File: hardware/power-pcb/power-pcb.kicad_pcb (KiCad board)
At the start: 2 copper layers, 165 x 48 mm, 71 parts, among them J1 XT60PW-M-AS, J10 Molex_MicroFit-3.0_4x1, J11 Molex_MicroFit-3.0_4x1, J12 Molex_MicroFit-3.0_4x1, J2 XT30, J3 MicroFit2x12_Odd_Even, J4 MicroFit2x12_CouterClockwise, J5 XT30, J6 XT30, J7 XT60PW-M-AS, J8 JST_XH_5, J9 Molex_MicroFit-3.0_4x1, Q1 SQJ138EP-T1_GE3, Q2 SQJ138EP-T1_GE3, U1 BTS50010-1TAD, U2 LTC4365TS8, U3 R-78E3.3-1.0, U4 BTT_TMC5160T_Pro, U5 BTT_TMC5160T_Pro, U6 BTT_TMC5160T_Pro, U7 BTT_TMC5160T_Pro

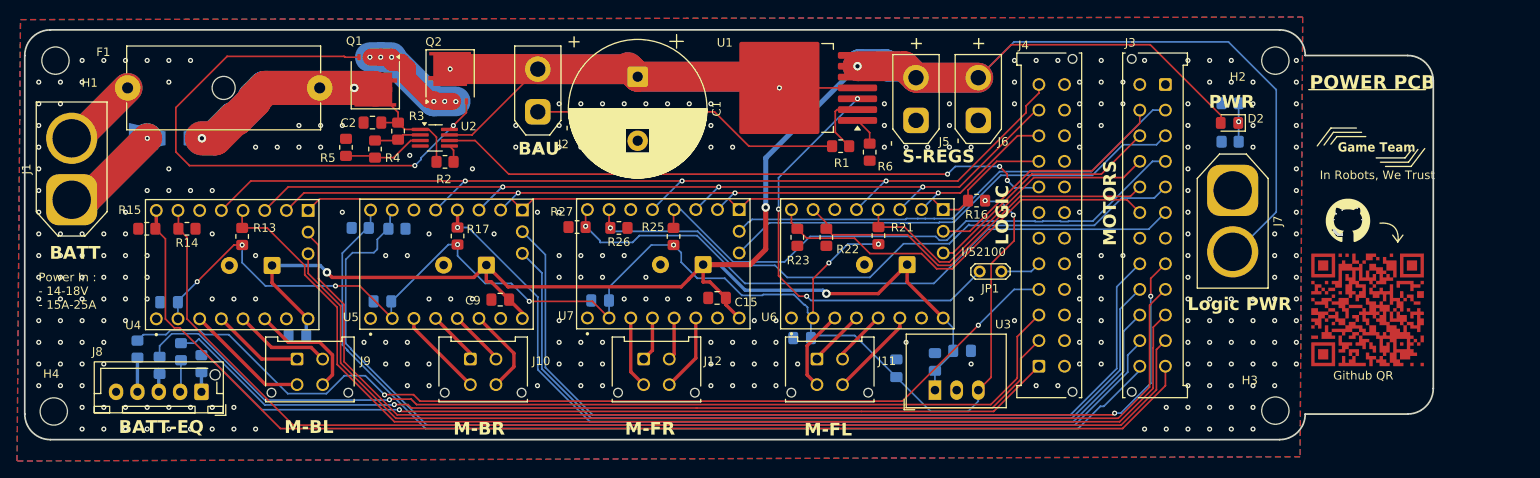
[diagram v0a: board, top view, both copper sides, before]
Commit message: Last fix power PCB
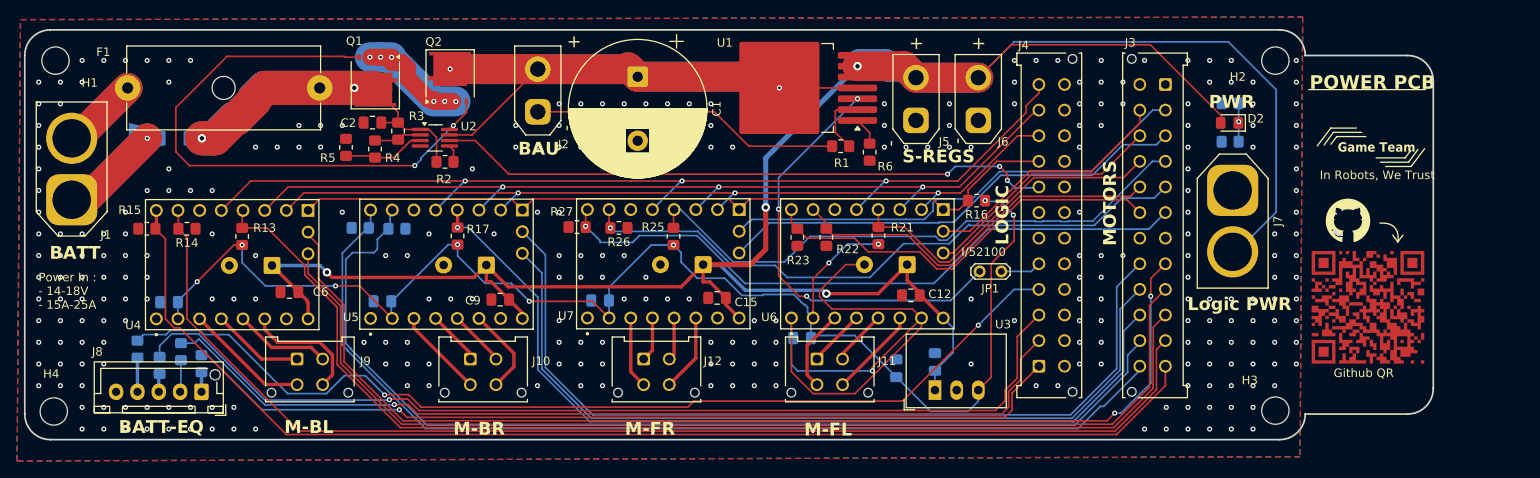
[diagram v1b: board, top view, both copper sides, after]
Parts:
- C12, C6: moved to F.Cu
- moved C12 8.85 mm to (143.9, 79.8), turned to 180 degrees
- moved C6 5.19 mm to (71.1, 79.4)
- moved QR***** 0.30 mm to (197.4, 81.2)
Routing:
- net GND: track 23.9 -> 94.6 mm, vias 291 -> 289
- net +BATT: track 288.7 -> 281.4 mm
- net /BATT_C4: track 103.0 -> 104.8 mm
- net /BATT_C3: track 108.8 -> 110.4 mm
- net /BATT_C2: track 115.6 -> 116.9 mm
- net /Motor_BL/MA: track 13.6 -> 14.4 mm
- net +3.3V: track 171.6 -> 170.9 mm
- net Net-(J2-Pin_1): track 36.8 -> 36.1 mm
- net /BL.CS: track 133.6 -> 134.2 mm
- net /BATT_C1: track 116.7 -> 117.3 mm
- net /BL.D1: track 125.5 -> 126.1 mm
- net /BL.D0: track 130.2 -> 130.8 mm
- net /FR.D0: track 55.8 -> 56.3 mm

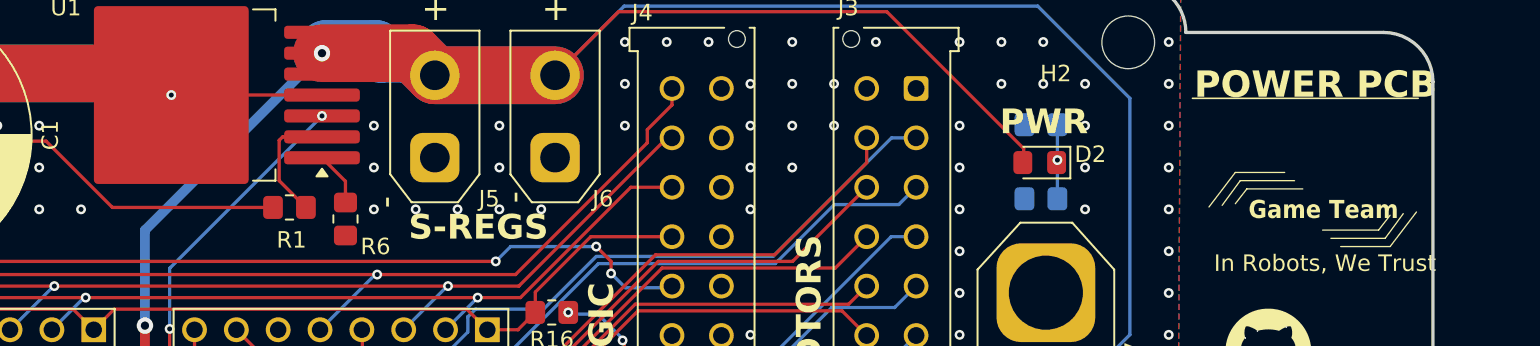
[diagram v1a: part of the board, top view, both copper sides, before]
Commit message: Post DRM adjustements and BOM referencing
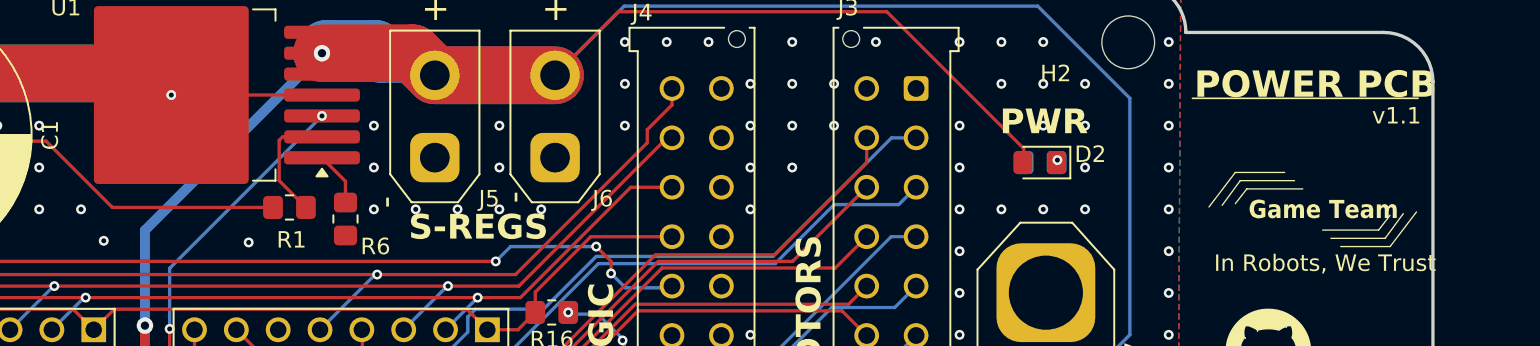
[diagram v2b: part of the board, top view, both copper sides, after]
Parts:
- removed R8: 2k, Resistor_SMD:R_0805_2012Metric_Pad1.20x1.40mm_HandSolder
- J1, J7: value XT60PW-M-AS -> XT60-M-AS
- R12: value 2k -> 1k
- moved R12 2.20 mm to (181.2, 59.6)
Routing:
- net Net-(D2-K): track 4.50 -> 0.00 mm
- net GND: vias 289 -> 294
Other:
- board text added: "v1.1"

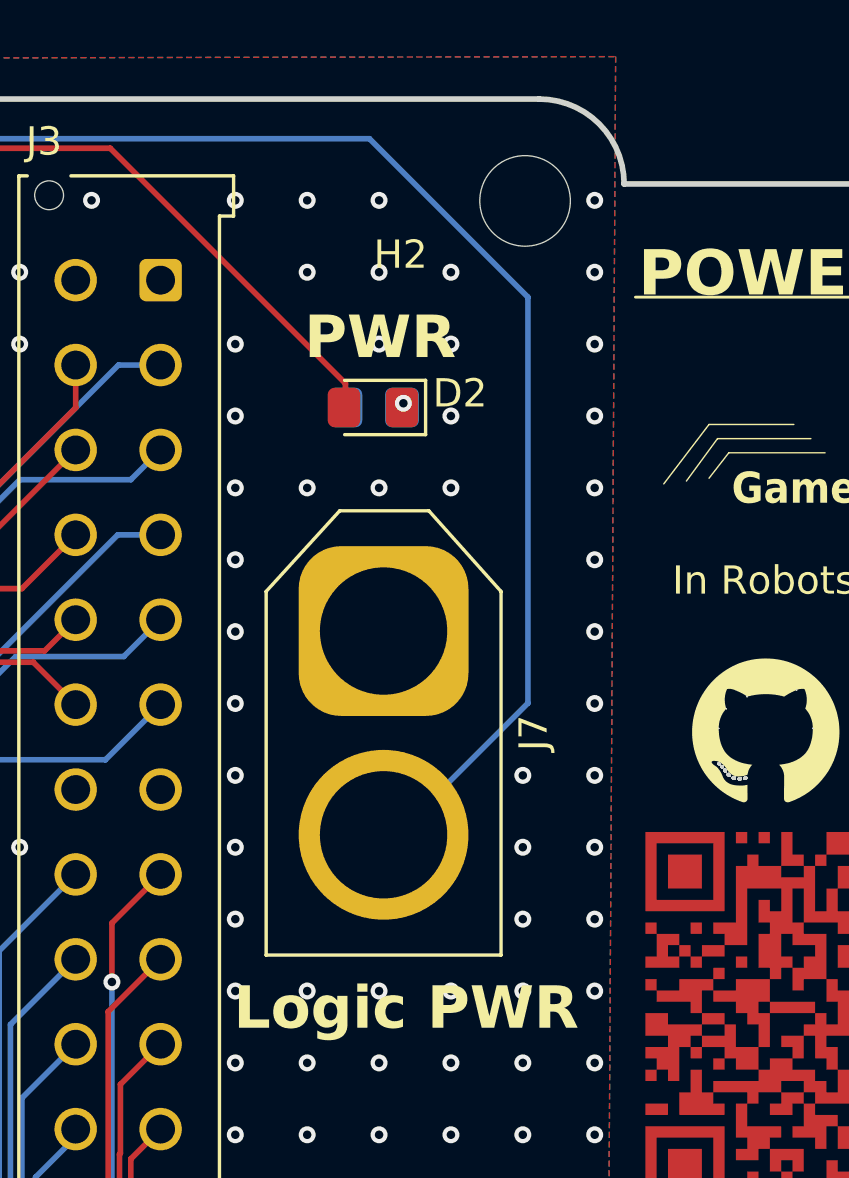
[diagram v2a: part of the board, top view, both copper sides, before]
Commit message: Change logic connector
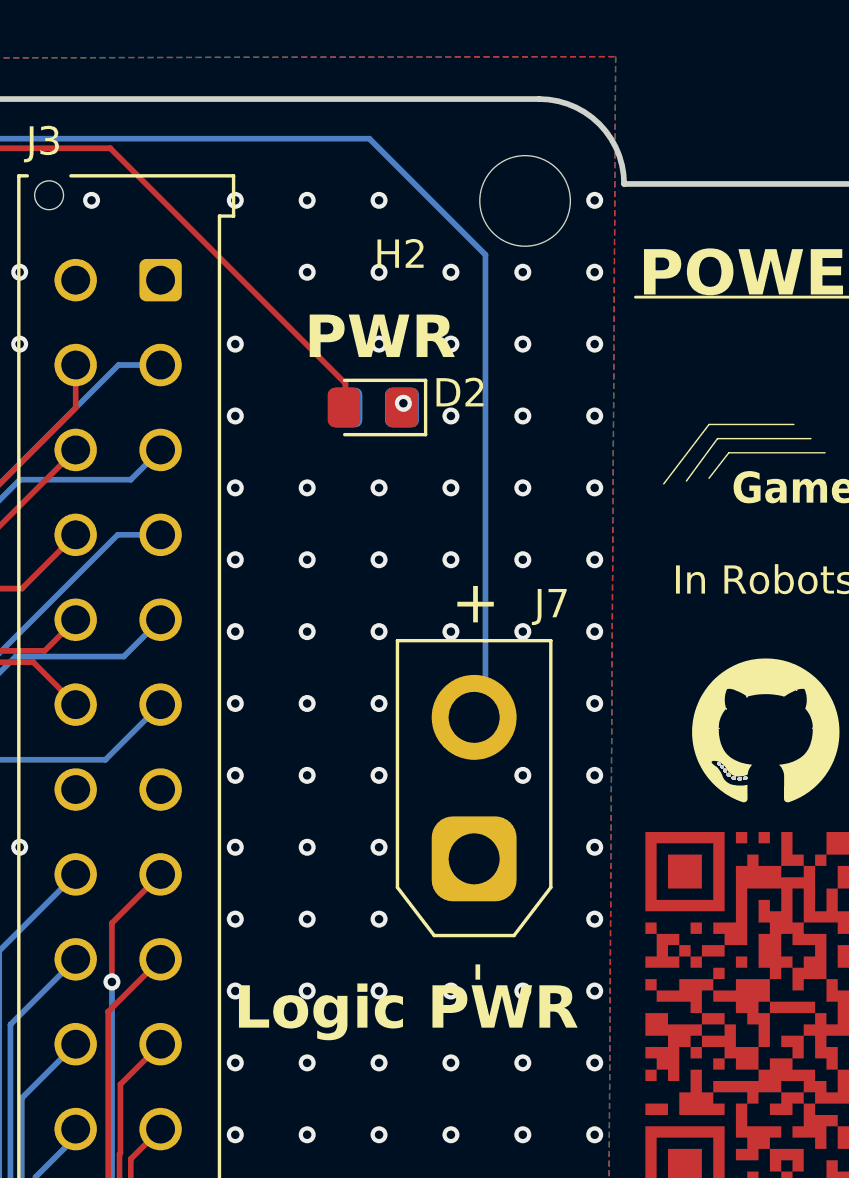
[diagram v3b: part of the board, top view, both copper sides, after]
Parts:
- J7: value XT60-M-AS -> XT30-M-AS; footprint Connector_AMASS:AMASS_XT60-M_1x02_P7.20mm_Vertical -> Project:AMASS_XT30UPB-M_1x02_P5.0mm_Vertical
- moved J7 8.66 mm to (184.8, 75.5), turned to 90 degrees
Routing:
- net +BATT: track 281.4 -> 274.3 mm
- net GND: vias 294 -> 312

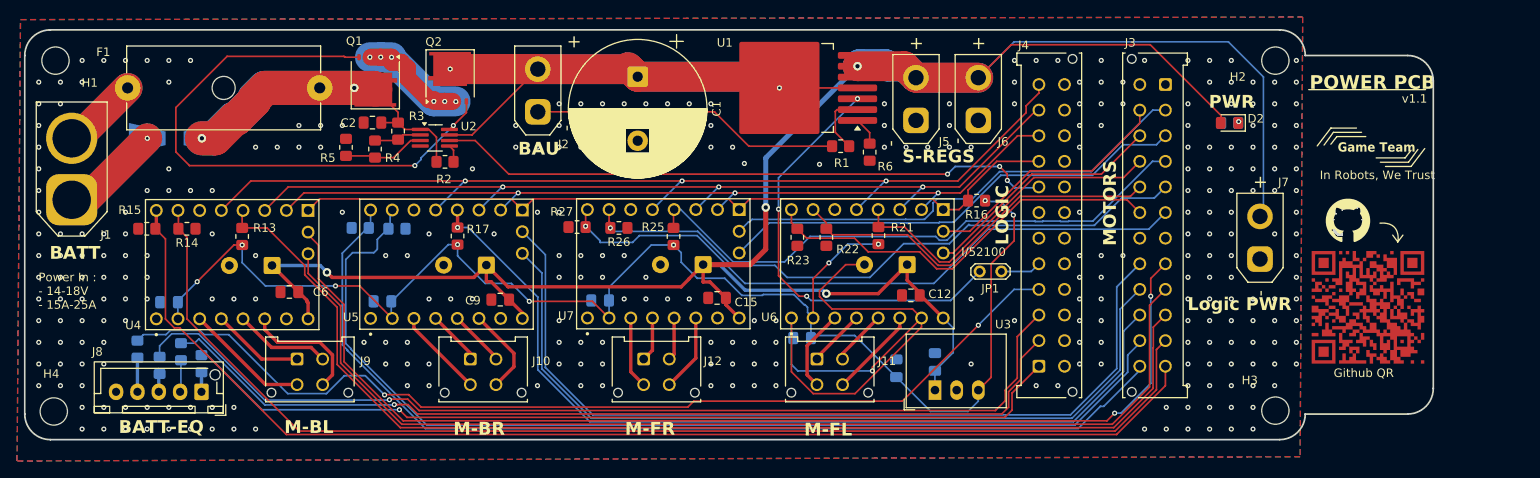
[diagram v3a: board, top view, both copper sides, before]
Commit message: Add shunt for current measure
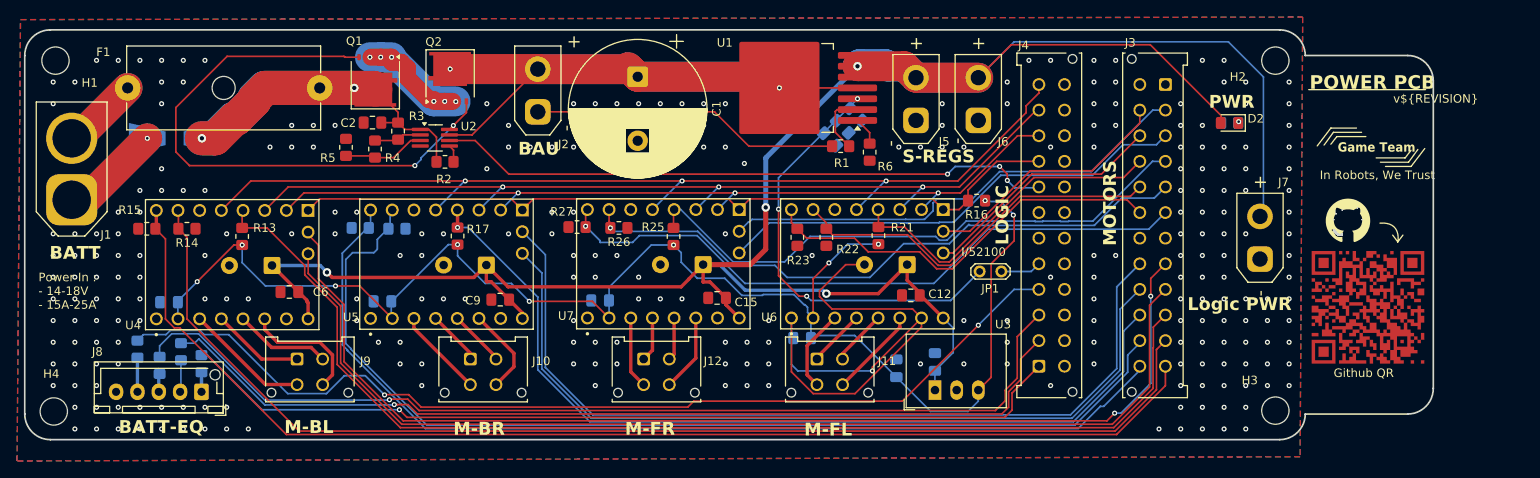
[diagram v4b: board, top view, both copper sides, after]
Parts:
- added C17: 100n, Capacitor_SMD:C_0805_2012Metric_Pad1.18x1.45mm_HandSolder, B.Cu at (134.4, 61.5)
- added R20: 10k, Resistor_SMD:R_0805_2012Metric_Pad1.20x1.40mm_HandSolder, B.Cu at (135.9, 60.1)
- added R8: 10k, Resistor_SMD:R_0805_2012Metric_Pad1.20x1.40mm_HandSolder, B.Cu at (137.4, 58.6)
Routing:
- net GND: vias 312 -> 280
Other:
- board text added: "v${REVISION}"
- board text removed: "v1.1"

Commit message: Adapt Power PCB to logic requirements
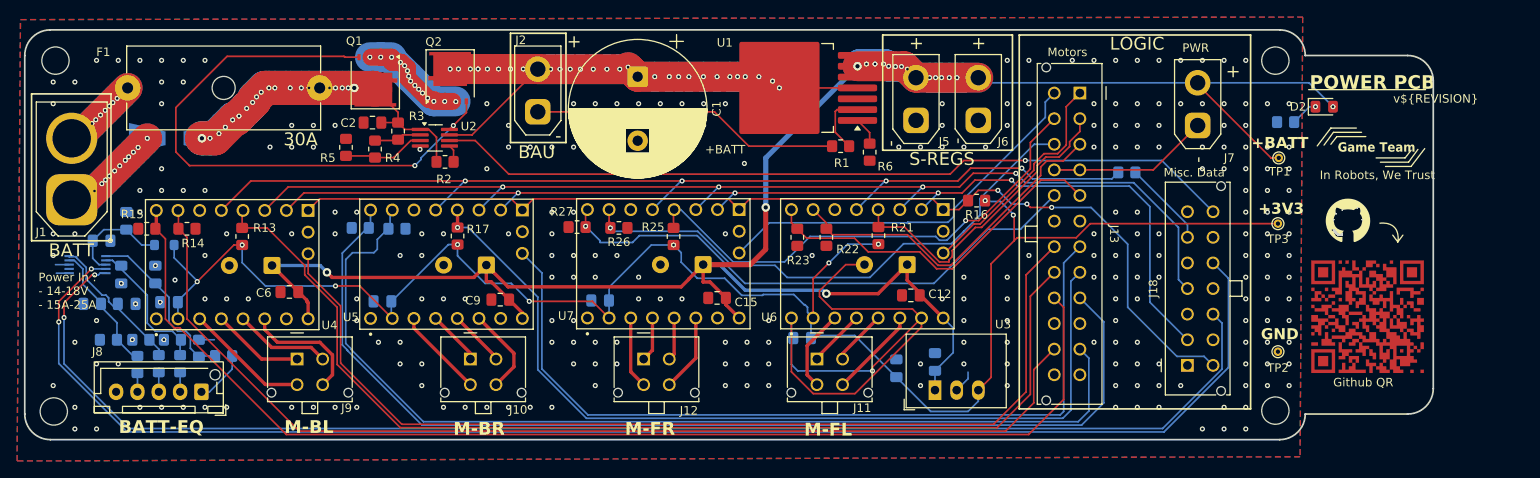
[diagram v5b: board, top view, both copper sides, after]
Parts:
- removed C17: 100n, Capacitor_SMD:C_0805_2012Metric_Pad1.18x1.45mm_HandSolder
- removed J3: MicroFit2x12_Odd_Even, Project:Molex_Micro-Fit_3.0_43045-2412_2x12_P3.00mm_Vertical
- removed J4: MicroFit2x12_CouterClockwise, Project:Molex_Micro-Fit_3.0_43045-2412_2x12_P3.00mm_Vertical
- removed JP1: Jumper_2_Bridged, Project:TestPoint_2Pads_Pitch2.54mm_Drill0.8mm
- removed R10, R11, R9: 1k, Resistor_SMD:R_0805_2012Metric_Pad1.20x1.40mm_HandSolder
- removed R20, R8: 10k, Resistor_SMD:R_0805_2012Metric_Pad1.20x1.40mm_HandSolder
- added C18: 10u, Capacitor_SMD:C_0805_2012Metric_Pad1.18x1.45mm_HandSolder, B.Cu at (52.0, 71.1)
- added C19: 100n, Capacitor_SMD:C_0805_2012Metric_Pad1.18x1.45mm_HandSolder, B.Cu at (49.1, 73.4)
- added C20: 100n, Capacitor_SMD:C_0805_2012Metric_Pad1.18x1.45mm_HandSolder, B.Cu at (48.0, 80.8)
- added C21: 100n, Capacitor_SMD:C_0805_2012Metric_Pad1.18x1.45mm_HandSolder, B.Cu at (52.0, 80.8)
- added C22: 100n, Capacitor_SMD:C_0805_2012Metric_Pad1.18x1.45mm_HandSolder, B.Cu at (51.4, 77.4)
- added C23: 100n, Capacitor_SMD:C_0805_2012Metric_Pad1.18x1.45mm_HandSolder, B.Cu at (55.4, 77.4)
- added FB1: BLM21PG331SN1D, Inductor_SMD:L_0805_2012Metric_Pad1.05x1.20mm_HandSolder, B.Cu at (56.5, 73.9)
- added J13: MicroFit2x12_Odd_Even, Project:J_Wurth_WR-MPC3_66202421122, F.Cu at (163.7, 56.1)
- added J18: Conn_02x07_Odd_Even, Project:J_Wurth_WR-MPC3_66201421122, F.Cu at (176.3, 88.0)
- added R39: 16.9k, Resistor_SMD:R_0805_2012Metric_Pad1.20x1.40mm_HandSolder, B.Cu at (53.3, 87.9)
- added R40: 59.0k, Resistor_SMD:R_0805_2012Metric_Pad1.20x1.40mm_HandSolder, B.Cu at (55.8, 87.8)
- added R41: 100k, Resistor_SMD:R_0805_2012Metric_Pad1.20x1.40mm_HandSolder, B.Cu at (58.3, 87.8)
- added R42: 24.9k, Resistor_SMD:R_0805_2012Metric_Pad1.20x1.40mm_HandSolder, B.Cu at (49.9, 85.0)
- added R46: 143k, Resistor_SMD:R_0805_2012Metric_Pad1.20x1.40mm_HandSolder, B.Cu at (63.4, 86.9)
- added R47: 24.9k, Resistor_SMD:R_0805_2012Metric_Pad1.20x1.40mm_HandSolder, B.Cu at (53.7, 85.0)
- added R48: 24.9K, Resistor_SMD:R_0805_2012Metric_Pad1.20x1.40mm_HandSolder, B.Cu at (57.4, 85.0)
- added R49: 24.9K, Resistor_SMD:R_0805_2012Metric_Pad1.20x1.40mm_HandSolder, B.Cu at (60.5, 86.0)
- added TP1: TestPoint, TestPoint:TestPoint_THTPad_D1.0mm_Drill0.5mm, F.Cu at (187.0, 63.7)
- added TP2: TestPoint, TestPoint:TestPoint_THTPad_D1.0mm_Drill0.5mm, F.Cu at (186.9, 86.4)
- added TP3: TestPoint, TestPoint:TestPoint_THTPad_D1.0mm_Drill0.5mm, F.Cu at (186.9, 71.4)
- added U8: ADS1015IDGS, Package_SO:TSSOP-10_3x3mm_P0.5mm, B.Cu at (47.5, 76.2)
- J10, J11, J12, J9: footprint Project:Molex_Micro-Fit_3.0_43045-0412_2x02_P3.00mm_Vertical -> Project:J_Wurth_WR-MPC3_66200421122
- J7: value XT30-M-AS -> XT30
- R7: value 1k -> 33R
- U1: value BTS50010-1TAD -> BTS50010-1TAE
- moved R7 110.7 mm to (169.2, 65.4), turned to 0 degrees
- moved J7 17.3 mm to (177.5, 59.9)
- moved D2 11.3 mm to (192.3, 57.7), turned to 0 degrees
- moved R12 6.55 mm to (187.8, 59.5)
- moved QR***** 1.10 mm to (197.4, 82.3)
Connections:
- net +3.3V renamed +3V3
- net /MSPI.MOSI renamed /MOSI
- net /MSPI.SCK renamed /SCK
- J8 pad 1: Net-(J8-Pin_1) -> /BATT_C4
- J8 pad 2: Net-(J8-Pin_2) -> /BATT_C3
- J8 pad 3: Net-(J8-Pin_3) -> /BATT_C2
- J8 pad 4: Net-(J8-Pin_4) -> /BATT_C1
- R7 pad 1: Net-(J8-Pin_1) -> /MISO
- R7 pad 2: /BATT_C4 -> Net-(J18-Pin_6)
- U1 pad 3: Net-(JP1-B) -> unconnected-(U1-IS-Pad3)
- U4 pad 17: /BL.D0 -> unconnected-(U4-DIAG0-Pad17)
- U4 pad 5: /MSPI.MISO -> /MISO
- U5 pad 17: /BR.D0 -> unconnected-(U5-DIAG0-Pad17)
- U5 pad 5: /MSPI.MISO -> /MISO
- U6 pad 17: /FL.D0 -> unconnected-(U6-DIAG0-Pad17)
- U6 pad 5: /MSPI.MISO -> /MISO
- U7 pad 17: /FR.D0 -> unconnected-(U7-DIAG0-Pad17)
- U7 pad 5: /MSPI.MISO -> /MISO
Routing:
- net /SDA_ACTUATION: track 0.00 -> 170.8 mm, vias 0 -> 2
- net /SCL_ACTUATION: track 0.00 -> 162.0 mm, vias 0 -> 2
- net /BL.D0: track 130.8 -> 0.00 mm, vias 2 -> 0
- net /MISO: track 0.00 -> 122.2 mm, vias 0 -> 4
- net /MSPI.MISO: track 117.2 -> 0.00 mm, vias 3 -> 0
- net /BATT_C1: track 117.3 -> 2.20 mm, vias 2 -> 0
- net /BATT_C2: track 116.9 -> 2.30 mm, vias 1 -> 0
- net /BATT_C3: track 110.4 -> 2.30 mm, vias 1 -> 0
- net /BR.D0: track 101.9 -> 0.00 mm
- net /BATT_C4: track 104.8 -> 6.24 mm, vias 1 -> 0
- net /FR.D0: track 56.3 -> 0.00 mm
- net Net-(JP1-B): track 50.7 -> 0.00 mm, vias 3 -> 0
- net +3V3: track 170.9 -> 208.0 mm
- net +BATT: track 274.3 -> 242.9 mm, vias 4 -> 17
- net /PROP_EN: track 92.0 -> 123.1 mm, vias 0 -> 3
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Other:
- board text added: "+3V3"
- board text added: "+BATT"
- board text added: "30A"
- board text added: "GND"
- board text added: "Misc. Data"
- board text added: "Motors"
- board text removed: "I/52100"
- board text removed: "Logic PWR"
- board text removed: "MOTORS"

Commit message: fixes pre-prod
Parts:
- J2, J5, J6, J7: footprint Project:AMASS_XT30UPB-M_1x02_P5.0mm_Vertical -> Project:AMASS_XT30U-M_1x02_P5.0mm_Vertical
- moved QR***** 0.32 mm to (197.3, 82.0)
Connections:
- J18 pad 10: /SCL_ACTUATION -> /SDA_ACTUATION
- J18 pad 12: /SDA_ACTUATION -> /SCL_ACTUATION
- J18 pad 14: /UOV_FAULT -> /PROP_EN
- J18 pad 2: /MOSI -> Net-(J18-Pin_2)
- J18 pad 6: Net-(J18-Pin_6) -> /MOSI
- J18 pad 8: /PROP_EN -> /UOV_FAULT
- R7 pad 2: Net-(J18-Pin_6) -> Net-(J18-Pin_2)
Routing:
- net /UOV_FAULT: track 94.2 -> 118.5 mm, vias 1 -> 2
- net Net-(J18-Pin_2): track 0.00 -> 21.8 mm, vias 0 -> 2
- net /MOSI: track 129.7 -> 118.1 mm
- net /PROP_EN: track 123.1 -> 111.8 mm, vias 3 -> 2
- net Net-(J18-Pin_6): track 10.1 -> 0.00 mm
- net /SCL_ACTUATION: track 162.0 -> 168.9 mm
- net /SDA_ACTUATION: track 170.8 -> 164.8 mm
- net GND: track 124.6 -> 130.0 mm, vias 287 -> 271
- net /SCK: track 130.4 -> 134.2 mm
- net +3V3: track 208.0 -> 209.0 mm
- net /UOV_BAU: vias 28 -> 26
- net +BATT: vias 17 -> 14
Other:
- board text added: "Rev ${REVISION}"
- board text removed: "v${REVISION}"
